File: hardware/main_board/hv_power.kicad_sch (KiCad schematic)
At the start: 28 parts, among them Q3 FDS2734, U11 LM5155

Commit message: hardware(sch): update hv boost output capacitor, update connector pinout
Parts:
- C36: value 0.47u/200V -> 10u/400v; footprint Capacitor_SMD:C_1206_3216Metric -> Capacitor_THT:C_Radial_D8.0mm_H11.5mm_P3.50mm; LCSC PN C725802 -> C46867081
- R32, R33: footprint Resistor_SMD:R_0603_1608Metric -> Resistor_SMD:R_0805_2012Metric
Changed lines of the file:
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@@
 			)
 		)
-		(property "Footprint" "Resistor_SMD:R_0603_1608Metric"
+		(property "Footprint" "Resistor_SMD:R_0805_2012Metric"
 			(at 228.6 81.28 0)
 			(effects
@@
 			)
 		)
-		(property "Value" "0.47u/200V"
+		(property "Value" "10u/400v"
 			(at 214.63 45.7262 0)
 			(effects
@@
 			)
 		)
-		(property "Footprint" "Capacitor_SMD:C_1206_3216Metric"
+		(property "Footprint" "Capacitor_THT:C_Radial_D8.0mm_H11.5mm_P3.50mm"
 			(at 212.09 44.45 0)
 			(effects
@@
 			)
 		)
-		(property "LCSC PN" "C725802"
+		(property "LCSC PN" "C46867081"
 			(at 212.09 44.45 0)
 			(effects
@@
 			)
 		)
-		(property "Footprint" "Resistor_SMD:R_0603_1608Metric"
+		(property "Footprint" "Resistor_SMD:R_0805_2012Metric"
 			(at 228.6 95.25 0)
 			(effects

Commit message: WIP(hardware): update in-4 display board
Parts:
- C36: footprint Capacitor_THT:C_Radial_D8.0mm_H11.5mm_P3.50mm -> johnson:Cap_THT_D8.0mm_L12mm_Horizontal
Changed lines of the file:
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@@
 			)
 		)
-		(property "Footprint" "Capacitor_THT:C_Radial_D8.0mm_H11.5mm_P3.50mm"
+		(property "Footprint" "johnson:Cap_THT_D8.0mm_L12mm_Horizontal"
 			(at 212.09 44.45 0)
 			(effects

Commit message: WIP(hardware): update main board and mainboard layout
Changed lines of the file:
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@@
-	)
-	(junction
-		(at 212.09 64.77)
-		(diameter 0)
-		(color 0 0 0 0)
 	)
 	(junction
@@
 		(pts
 			(xy 195.58 29.21) (xy 204.47 29.21)
-		)
-		(stroke
-			(width 0)
-			(type default)
-		)
-	)
-	(wire
-		(pts
-			(xy 212.09 64.77) (xy 260.35 64.77)
 		)
 		(stroke
@@
 		)
 	)
-	(hierarchical_label "PWR_VIN-"
+	(hierarchical_label "GND"
 		(shape input)
 		(at 45.72 80.01 180)
@@
 		)
 	)
-	(hierarchical_label "PWR_HV-"
-		(shape input)
-		(at 260.35 64.77 0)
-		(effects
-			(font
-				(size 1.27 1.27)
-			)
-			(justify left)
-		)
-	)

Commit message: chore(hardware): update bom and LCSC SN
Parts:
- R32: LCSC PN (none) -> C107700
- R33: LCSC PN C217952 -> C2828725
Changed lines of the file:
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@@
 			)
 		)
-		(property "LCSC PN" ""
+		(property "LCSC PN" "C107700"
 			(at 228.6 81.28 0)
 			(effects
@@
 			)
 		)
-		(property "LCSC PN" "C217952"
+		(property "LCSC PN" "C2828725"
 			(at 228.6 95.25 0)
 			(effects

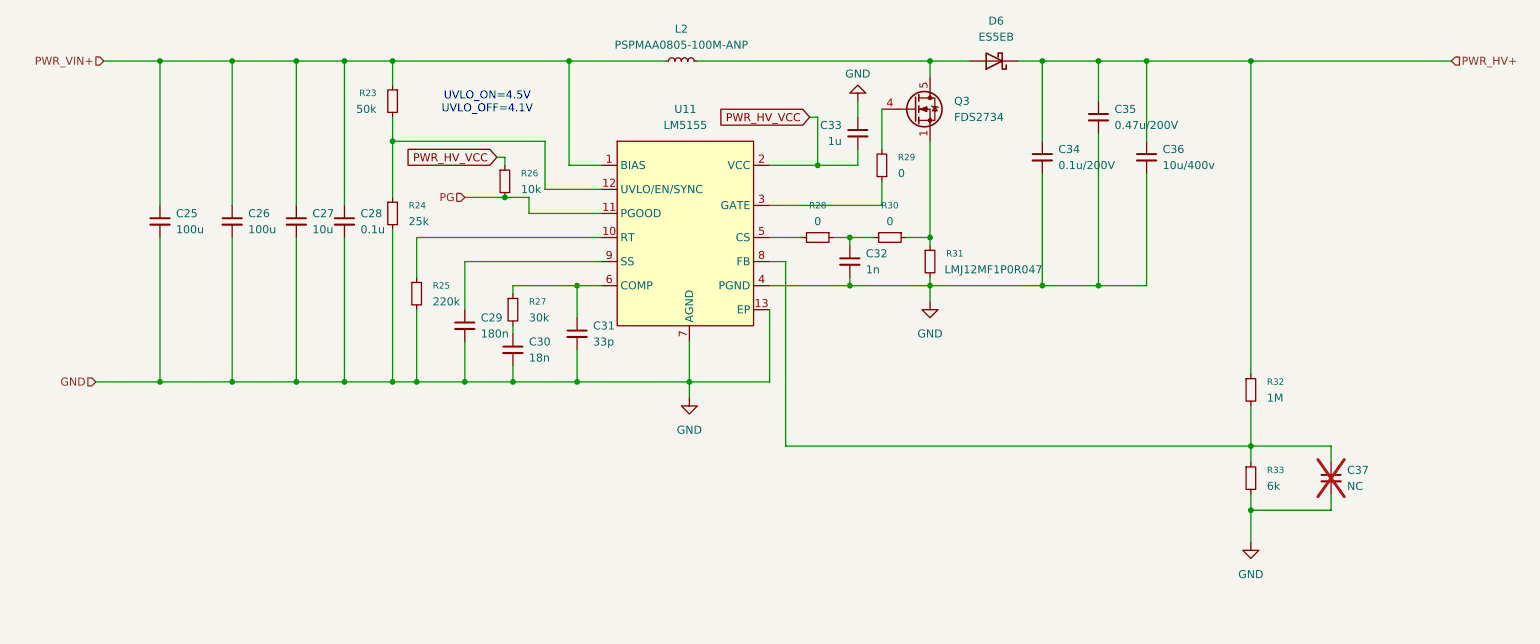
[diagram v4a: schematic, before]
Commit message: hardware(schematic): update main control board schematic and layout
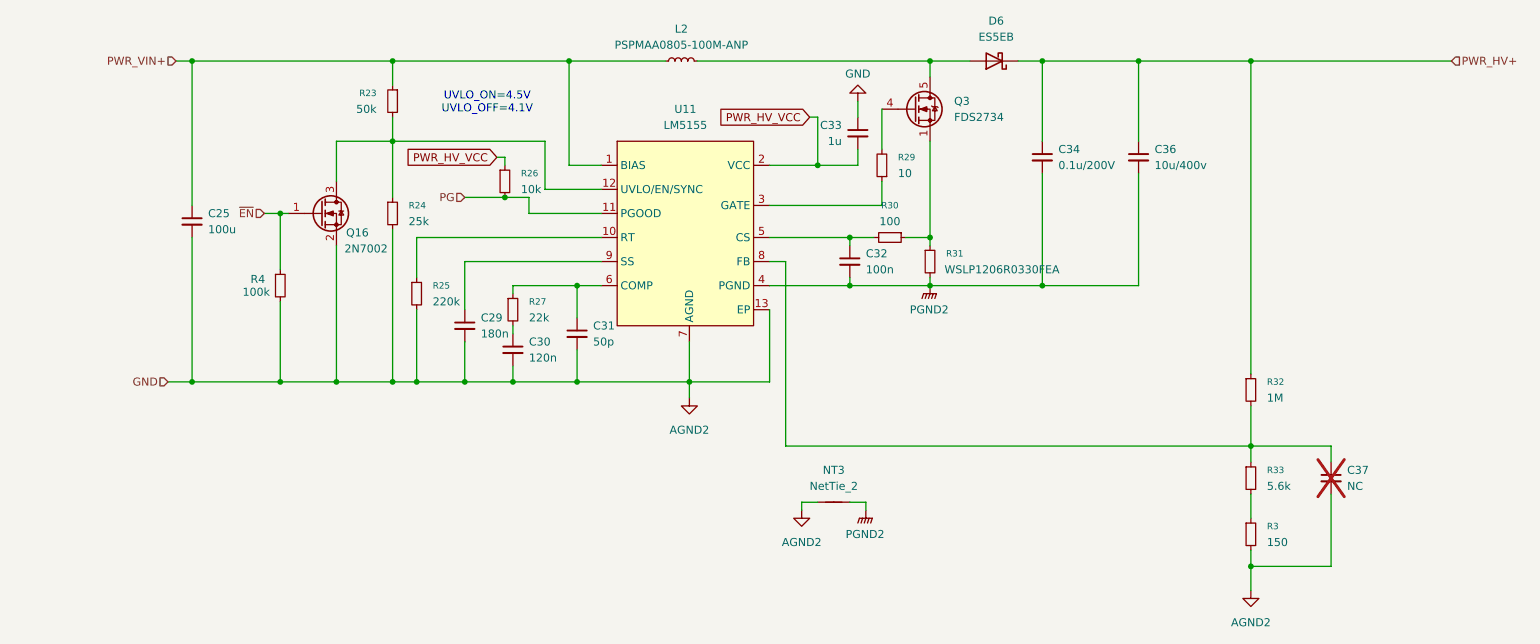
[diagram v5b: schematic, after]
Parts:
- removed C26: 100u, Capacitor_SMD:C_1206_3216Metric, symbol Device:C_Small
- removed C27: 10u, Capacitor_SMD:C_0603_1608Metric, symbol Device:C_Small
- removed C28: 0.1u, Capacitor_SMD:C_0603_1608Metric, symbol Device:C_Small
- removed C35: 0.47u/200V, Capacitor_SMD:C_1206_3216Metric, symbol Device:C_Small
- removed R28: 0, Resistor_SMD:R_0603_1608Metric, symbol Device:R_Small
- added NT3: NetTie_2, NetTie:NetTie-2_SMD_Pad0.5mm, symbol Device:NetTie_2
- added Q16: 2N7002, Package_TO_SOT_SMD:SOT-23, symbol Transistor_FET:2N7002
- added R3: 150, Resistor_SMD:R_0603_1608Metric, symbol Device:R_Small
- added R4: 100k, Resistor_SMD:R_0603_1608Metric, symbol Device:R_Small
- C29: LCSC PN C519442 -> C519440
- C30: value 18n -> 120n; LCSC PN C519551 -> C237177
- C31: value 33p -> 50p; LCSC PN C107047 -> C576819
- C32: value 1n -> 100n; LCSC PN C100040 -> C14663
- C33: LCSC PN C106248 -> C5199872
- R25: LCSC PN C217882 -> C22961
- R27: value 30k -> 22k; LCSC PN C2828685 -> C114065
- R29: value 0 -> 10; LCSC PN C304185 -> C22859
- R30: value 0 -> 100; LCSC PN C304185 -> C22775
- R31: value LMJ12MF1P0R047 -> WSLP1206R0330FEA; LCSC PN C5121701 -> C2084257
- R32: footprint Resistor_SMD:R_0805_2012Metric -> Resistor_SMD:R_0603_1608Metric; LCSC PN C107700 -> C22935
- R33: value 6k -> 5.6k; footprint Resistor_SMD:R_0805_2012Metric -> Resistor_SMD:R_0603_1608Metric; LCSC PN C2828725 -> C23189
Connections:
- net at R23.2, R24.1, U11.12 (UVLO/EN/SYNC): now also Q16.3 (D)
- net at C32.1, R30.2: now also U11.5 (CS)
- net GND renamed AGND2
- net AGND2: now also NT3.1, Q16.2 (S), R3.2, R4.2; no longer C32.2, C34.2, C36.2, R31.2, R33.2, U11.4 (PGND)
- new net: R3.1, R33.2
- new net PGND2: C32.2, C34.2, C36.2, NT3.2, R31.2, U11.4 (PGND)
- new net ~{EN}: Q16.1 (G), R4.1
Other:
- moved on the sheet: C25, C36

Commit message: chore(sch): adjust 3v3, 5v and power switch solutions.
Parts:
- removed Q16: 2N7002, Package_TO_SOT_SMD:SOT-23, symbol Transistor_FET:2N7002
- removed R4: 100k, Resistor_SMD:R_0603_1608Metric, symbol Device:R_Small
